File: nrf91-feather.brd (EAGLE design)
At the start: 50.8 x 22.9 mm, 125 parts, among them J1 CON-USB-1050170001, J2 CON-HEADER-1X12-MALE-PIN, J3 CON-HEADER-1X16-MALE-PIN, J4 CON-1909763-1, J5 CON-SIM-104224-0820, J6 CON-S2B-PH-SM4-TB(LF)(SN), J7 CON-1909763-1, J9 CON-TC2030-MCP-NL, Q1 MOSFET-P-SC89, Q2 MOSFET-DUAL-COMP-SOT563, Q3 MOSFET-P-20V-4.7A-SOT23, Q4 MOSFET-N-SC89, Q5 MOSFET-N-SC89, SW1 SW-EVP-AA402W, SW2 SW-EVP-AA402W, U1 MOD-NRF9160-SICA-R, U10 IC-LIS2DH12TR, U2 IC-CP2102N-A02-GQFN20R, U3 IC-TPS63031DSKR, U4 POWER-SWITCH-MIC94092YC6, U5 IC-TPD4S012DRYR, U6 FLASH-W25Q32JVZPIQ-WSON, U7 IC-STBC08PMR, U8 IC-PCF85063ATL/1, U9 IC-BAV70S, Y1 XTAL-ABS07AIG-32.768KHZ-7-T

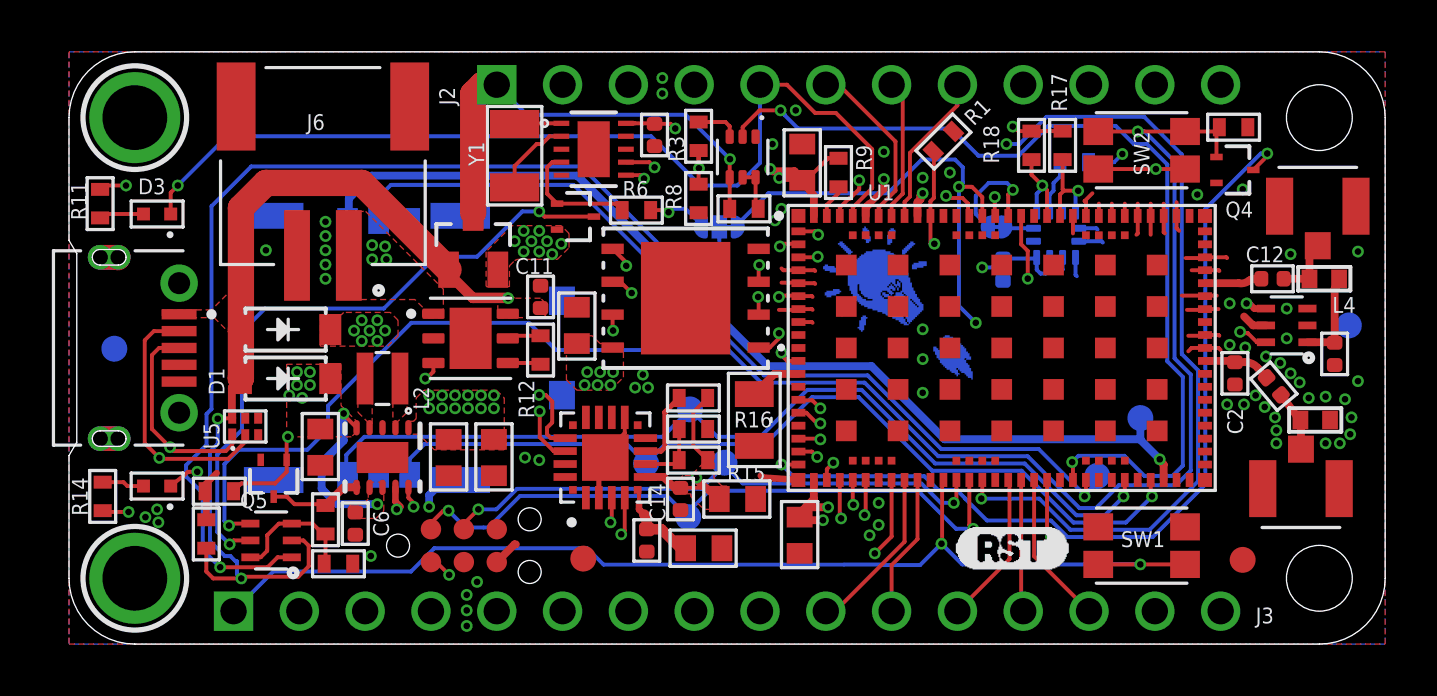
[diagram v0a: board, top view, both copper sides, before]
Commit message: Adding accelerometer INT2 pin connection.
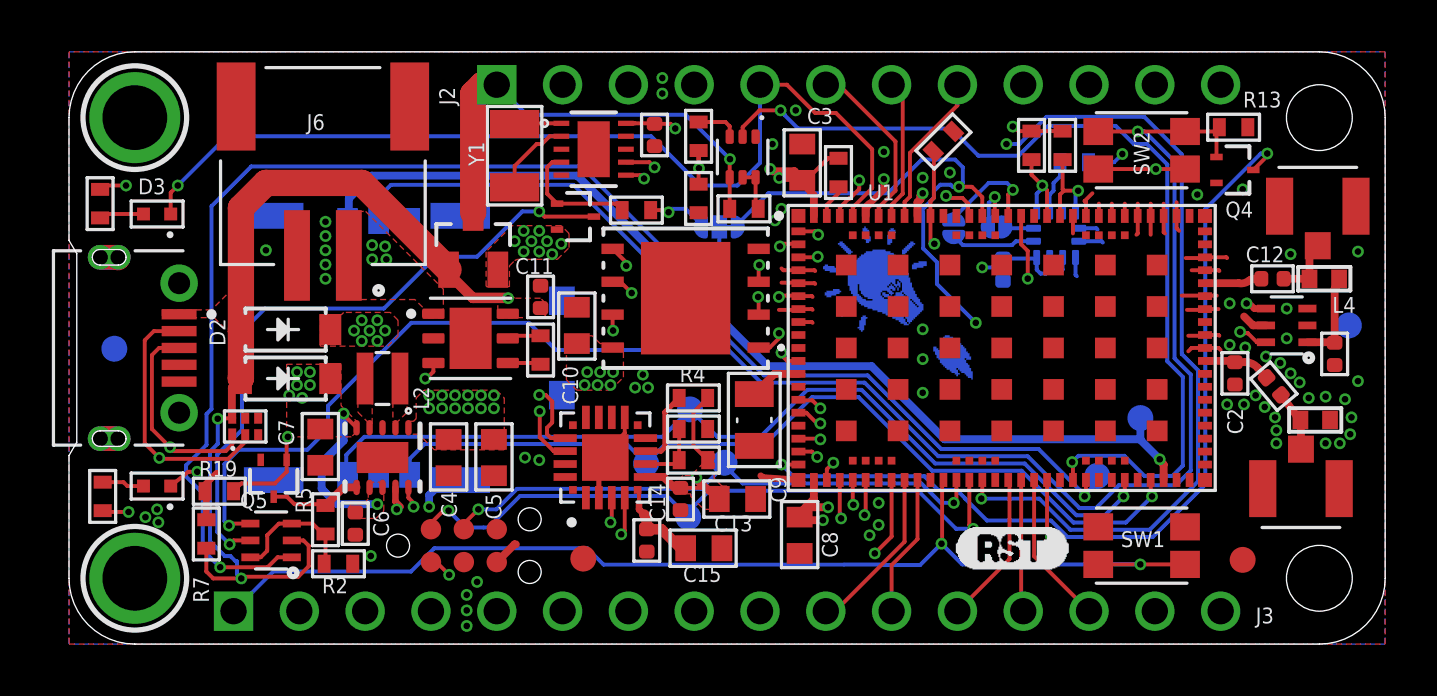
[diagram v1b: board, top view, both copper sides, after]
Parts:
- added JMP3: JUMPER-NO-ROUND-NO, wolff-den:JUMPER-ROUND-N0
- JMP1: value JUMPER-NC -> JUMPER-NO-ROUND-NO; device wolff-den:JUMPER-ROUND-NC -> wolff-den:JUMPER-ROUND-N0
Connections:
- new net N$12: JMP3.P$1, U10.11
- net P0.29/D2: now also JMP3.P$2; no longer JMP1.P$2
- net P0.30/D3: now also JMP1.P$2
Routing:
- net N$12: track 0.00 -> 3.28 mm
- net P0.31/NRF_PS_EN: track 33.7 -> 35.3 mm
- net P0.30/D3: track 5.98 -> 7.24 mm

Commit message: Optimizing power layout
Changed:
* Created large power paths on middle layers (power an return)
* Pin7 on power supply chip to ground (power save mode/pfm enabled)
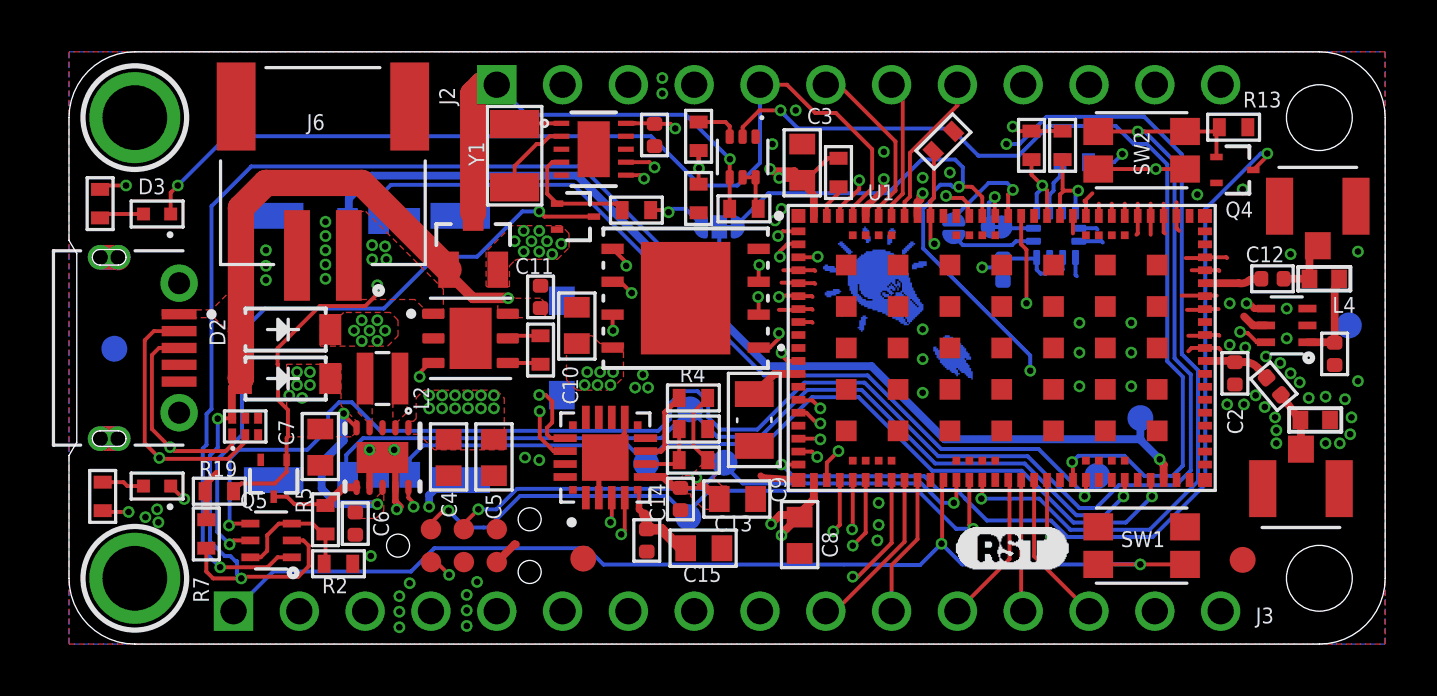
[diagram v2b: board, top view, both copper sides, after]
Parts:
- JMP1: value JUMPER-NO-ROUND-NO -> JUMPER-NC; device wolff-den:JUMPER-ROUND-N0 -> wolff-den:JUMPER-ROUND-NC
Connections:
- net GND: now also U3.7
- net VSYS: no longer U3.7
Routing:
- net GND: track 44.8 -> 47.1 mm, vias 68 -> 82
- net P0.13/A0: track 16.1 -> 18.3 mm
- net VBUS: track 55.1 -> 53.7 mm
- net P0.05/USB_UART_RX: track 19.4 -> 17.9 mm
- net DIFF_P: track 28.5 -> 27.1 mm
- net DIFF_N: track 31.8 -> 30.6 mm
- net !EN: track 22.6 -> 23.7 mm
- net FLASH_SO: track 13.9 -> 14.8 mm
- net MODE/WAKE: track 73.6 -> 74.2 mm
- net P0.16/A3: track 10.5 -> 9.91 mm
- net FLASH_WP: track 9.42 -> 8.85 mm
- net NRF_PS_EN_JMP: track 40.2 -> 39.6 mm

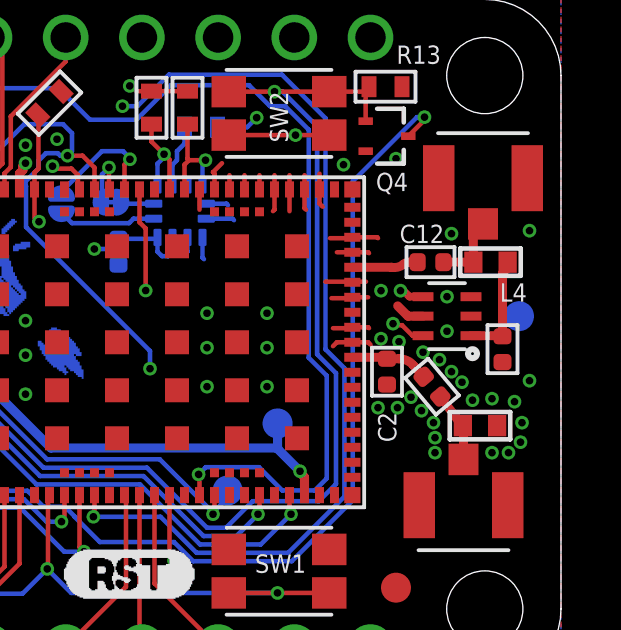
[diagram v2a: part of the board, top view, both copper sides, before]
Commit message: Replacing U4 with 2.8V regulator.
Changed:
* U4 to MIC5365-2.8YC5-TR
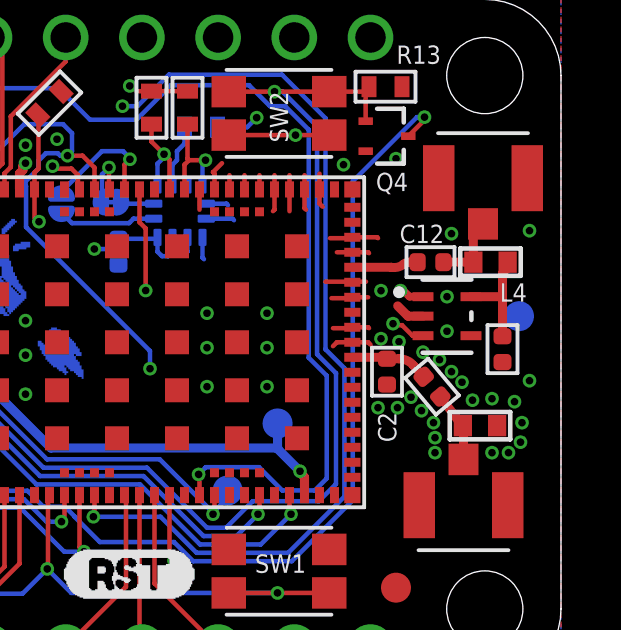
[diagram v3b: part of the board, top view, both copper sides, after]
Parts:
- U4: value POWER-SWITCH-MIC94092YC6 -> (none); device wolff-den:SOT363 -> wolff-den:SOT353
- turned U4 to 0 degrees
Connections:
- net +3V3: now also U4.1; no longer U4.4
- net COEX0/LNA_EN: now also U4.3; no longer U4.6
- net GND: no longer U4.5
- net LNA_SW_OUT: now also U4.5; no longer U4.1
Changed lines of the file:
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@@
 <layer number="29" name="tStop" color="7" fill="3" visible="no" active="yes"/>
 <layer number="30" name="bStop" color="7" fill="6" visible="no" active="yes"/>
-<layer number="31" name="tCream" color="7" fill="4" visible="no" active="yes"/>
+<layer number="31" name="tCream" color="7" fill="4" visible="yes" active="yes"/>
 <layer number="32" name="bCream" color="7" fill="5" visible="no" active="yes"/>
 <layer number="33" name="tFinish" color="6" fill="3" visible="no" active="yes"/>
@@
 <layer number="49" name="Reference" color="7" fill="1" visible="no" active="yes"/>
 <layer number="50" name="dxf" color="7" fill="1" visible="no" active="no"/>
-<layer number="51" name="tDocu" color="7" fill="1" visible="yes" active="yes"/>
+<layer number="51" name="tDocu" color="7" fill="1" visible="no" active="yes"/>
 <layer number="52" name="bDocu" color="7" fill="1" visible="no" active="yes"/>
 <layer number="53" name="tGND_GNDA" color="7" fill="9" visible="no" active="no"/>
@@
 <attribute name="TOLERANCE" value="5%" x="5.8" y="5.9" size="1.778" layer="27" display="off"/>
 </element>
-<element name="U4" library="wolff-den" library_urn="urn:adsk.eagle:library:6370453" package="SOT363" package3d_urn="urn:adsk.eagle:package:5807345/9" value="POWER-SWITCH-MIC94092YC6" x="47" y="12.3" smashed="yes" rot="R90">
-<attribute name="DESC" value="IC LOAD SW HGH SIDE 1.2A SC70-6" x="47" y="12.3" size="1.778" layer="27" rot="R90" display="off"/>
-<attribute name="DIGIKEYPN" value="576-3488-1-ND" x="47" y="12.3" size="1.778" layer="27" rot="R90" display="off"/>
-<attribute name="MPN" value="MIC94092YC6-TR" x="47" y="12.3" size="1.778" layer="27" rot="R90" display="off"/>
-<attribute name="NAME" x="45.0465" y="12.34428125" size="0.6096" layer="25" font="vector" ratio="20" rot="R90"/>
-<attribute name="NAME" x="47" y="12.3" size="0.2" layer="51" rot="R90" align="center"/>
+<element name="U4" library="wolff-den" library_urn="urn:adsk.eagle:library:6370453" package="SOT353" package3d_urn="urn:adsk.eagle:package:19061981/1" value="" x="47" y="12.3" smashed="yes">
+<attribute name="DESC" value="IC REG LINEAR 2.8V 150MA SC70-5" x="47" y="12.3" size="1.778" layer="27" display="off"/>
+<attribute name="DIGIKEYPN" value="576-3187-1-ND" x="47" y="12.3" size="1.778" layer="27" display="off"/>
+<attribute name="MPN" value="MIC5365-2.8YC5-TR" x="47" y="12.3" size="1.778" layer="27" display="off"/>
+<attribute name="NAME" x="45.0965" y="11.89428125" size="0.6096" layer="25" font="vector" ratio="20" rot="R90"/>
+<attribute name="NAME" x="47" y="12.3" size="0.2" layer="51" align="center"/>
 </element>
 <element name="C2" library="wolff-den" library_urn="urn:adsk.eagle:library:6370453" package="CAPC1005X55N" package3d_urn="urn:adsk.eagle:package:7419912/5" value="15p" x="45" y="10.45" smashed="yes" rot="R270">
@@
 <wire x1="5.25" y1="5.9" x2="5.25" y2="6.15" width="0.254" layer="1"/>
 <wire x1="5.25" y1="6.15" x2="5.7" y2="6.6" width="0.254" layer="1"/>
-<contactref element="U4" pad="5"/>
 <contactref element="U4" pad="2"/>
 <via x="44.8" y="13.15" extent="1-16" drill="0.254"/>
@@
 <wire x1="36.45" y1="20" x2="36.425" y2="19.975" width="0.1524" layer="1"/>
 <via x="36.425" y="19.975" extent="1-16" drill="0.254"/>
-<contactref element="U4" pad="4"/>
+<contactref element="U4" pad="1"/>
 <wire x1="45.45" y1="13.15" x2="45.55" y2="13.15" width="0.254" layer="1"/>
 <wire x1="45.75" y1="12.95" x2="45.55" y2="13.15" width="0.254" layer="1"/>
@@
 <wire x1="33.4" y1="15.45" x2="33.8794" y2="14.9706" width="0.1524" layer="2"/>
 <contactref element="R1" pad="2"/>
-<contactref element="U4" pad="6"/>
+<contactref element="U4" pad="3"/>
 <wire x1="46.2" y1="11.65" x2="45.85" y2="11.65" width="0.1524" layer="1"/>
 <wire x1="45.2" y1="12.05" x2="45.1842" y2="12.05" width="0.1524" layer="2"/>
@@
 <contactref element="L4" pad="1"/>
 <contactref element="C19" pad="1"/>
-<contactref element="U4" pad="1"/>
+<contactref element="U4" pad="5"/>
 <wire x1="49.11075" y1="14.01075" x2="49.11075" y2="13.98925" width="0.254" layer="1"/>
 <wire x1="48.85" y1="11.63" x2="48.83" y2="11.65" width="0.3" layer="1"/>
-<wire x1="48.83" y1="11.65" x2="47.8" y2="11.65" width="0.3" layer="1"/>
 <wire x1="49.11075" y1="13.98925" x2="48.85" y2="13.7285" width="0.3" layer="1"/>
-<wire x1="48.85" y1="11.63" x2="48.85" y2="13.7285" width="0.3" layer="1"/>
+<wire x1="48.85" y1="11.63" x2="48.85" y2="12.95" width="0.3" layer="1"/>
+<wire x1="48.85" y1="12.95" x2="48.85" y2="13.7285" width="0.3" layer="1"/>
 <wire x1="49.0215" y1="14.1" x2="49.11075" y2="14.01075" width="0.3" layer="1"/>
+<wire x1="47.8" y1="12.95" x2="48.85" y2="12.95" width="0.3" layer="1"/>
 </signal>
 <signal name="GPS_ANT" class="2">

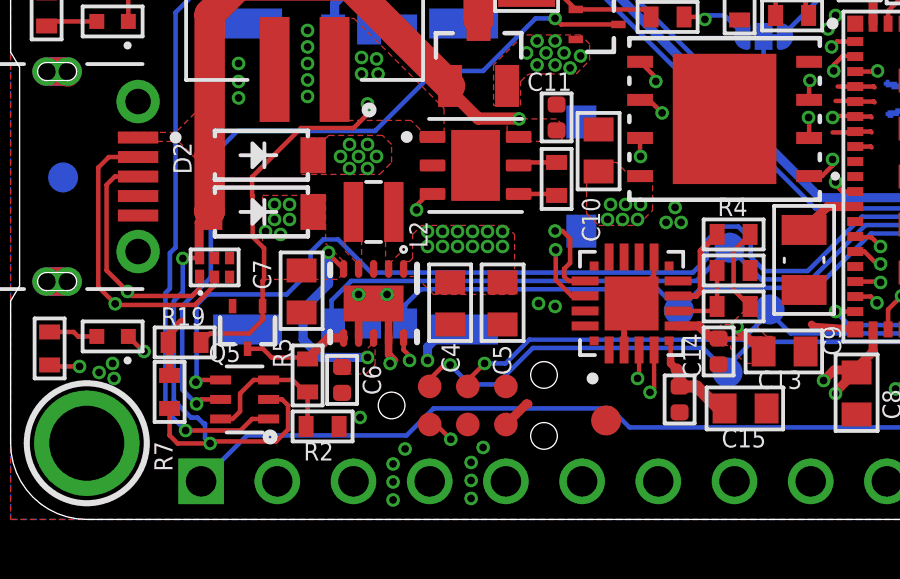
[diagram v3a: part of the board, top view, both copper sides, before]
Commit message: Comparing and fixing U3 connections
Changed:
* U3.8 should not be connected to VSYS. Now the same as a few reference designs i've seen.
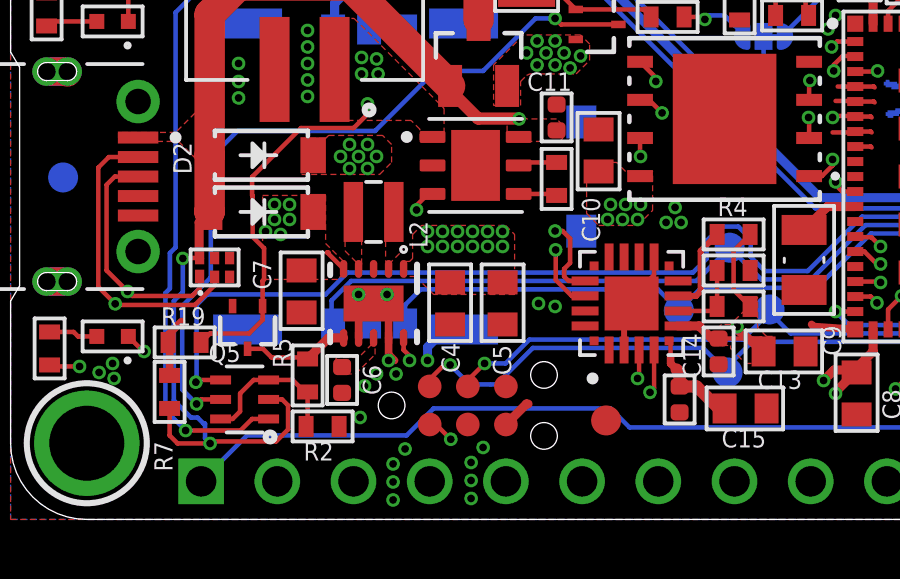
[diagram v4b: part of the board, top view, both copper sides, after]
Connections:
- new net N$14: C6.1, U3.8
- net VSYS: no longer C6.1, U3.8
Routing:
- net VSYS: track 60.7 -> 54.0 mm, vias 20 -> 18
- net MODE/WAKE: track 74.2 -> 72.9 mm
- net GND: vias 82 -> 85
- added copper zone on layer 1, net N$14
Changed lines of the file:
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@@
 <layer number="29" name="tStop" color="7" fill="3" visible="no" active="yes"/>
 <layer number="30" name="bStop" color="7" fill="6" visible="no" active="yes"/>
-<layer number="31" name="tCream" color="7" fill="4" visible="yes" active="yes"/>
+<layer number="31" name="tCream" color="7" fill="4" visible="no" active="yes"/>
 <layer number="32" name="bCream" color="7" fill="5" visible="no" active="yes"/>
 <layer number="33" name="tFinish" color="6" fill="3" visible="no" active="yes"/>
@@
 <layer number="49" name="Reference" color="7" fill="1" visible="no" active="yes"/>
 <layer number="50" name="dxf" color="7" fill="1" visible="no" active="no"/>
-<layer number="51" name="tDocu" color="7" fill="1" visible="no" active="yes"/>
+<layer number="51" name="tDocu" color="7" fill="1" visible="yes" active="yes"/>
 <layer number="52" name="bDocu" color="7" fill="1" visible="no" active="yes"/>
 <layer number="53" name="tGND_GNDA" color="7" fill="9" visible="no" active="no"/>
@@
 <via x="21.85" y="9.9" extent="1-16" drill="0.254"/>
 <via x="22.15" y="10.4" extent="1-16" drill="0.254"/>
-<via x="12.65" y="5.2" extent="1-16" drill="0.254"/>
+<via x="12.6" y="5.3" extent="1-16" drill="0.254"/>
 <via x="11.65" y="3.4" extent="1-16" drill="0.254"/>
 <wire x1="30.75" y1="16.525" x2="30.75" y2="16.8471" width="0.3048" layer="1"/>
@@
 <via x="7.6" y="14.6" extent="1-16" drill="0.254"/>
 <via x="7.6" y="14.05" extent="1-16" drill="0.254"/>
+<via x="12.2" y="4.85" extent="1-16" drill="0.254"/>
+<via x="11.8" y="4.45" extent="1-16" drill="0.254"/>
+<via x="12.85" y="4.85" extent="1-16" drill="0.254"/>
 </signal>
 <signal name="+3V3">
@@
 <contactref element="D1" pad="1"/>
 <contactref element="C7" pad="1"/>
-<contactref element="C6" pad="1"/>
 <contactref element="U3" pad="5"/>
-<contactref element="U3" pad="8"/>
-<via x="11.9" y="5.4" extent="1-16" drill="0.254"/>
 <polygon width="0.1524" layer="1" thermals="no">
 <vertex x="10.9" y="8"/>
@@
 <via x="19" y="15.45" extent="1-16" drill="0.254"/>
 <via x="8.5" y="9.6" extent="1-16" drill="0.254"/>
-<polygon width="0.1524" layer="1" thermals="no">
-<vertex x="10.85" y="5.4"/>
-<vertex x="10.85" y="4.85"/>
-<vertex x="11.85" y="4.85"/>
-<vertex x="12.15" y="5.15"/>
-<vertex x="12.15" y="6.25"/>
-<vertex x="12.05" y="6.25"/>
-<vertex x="12.05" y="5.85"/>
-<vertex x="11.6" y="5.4"/>
-</polygon>
 <contactref element="SW2" pad="3"/>
 <contactref element="SW2" pad="1"/>
@@
 <wire x1="11.100003125" y1="8.35" x2="10.550003125" y2="8.9" width="0.1524" layer="1"/>
 <wire x1="10.550003125" y1="8.9" x2="10.6" y2="8.9" width="0.1524" layer="1"/>
-<via x="10.6" y="8.9" extent="1-16" drill="0.254"/>
-<wire x1="10.6" y1="8.9" x2="10.6" y2="7.85" width="0.3048" layer="16"/>
-<wire x1="10.6" y1="7.85" x2="9.75" y2="7" width="0.3048" layer="16"/>
-<wire x1="9.75" y1="7" x2="9.75" y2="6" width="0.3048" layer="16"/>
-<wire x1="10.35" y1="5.4" x2="11.9" y2="5.4" width="0.3048" layer="16"/>
-<wire x1="9.75" y1="6" x2="10.35" y2="5.4" width="0.3048" layer="16"/>
-<wire x1="10.6" y1="8.9" x2="10.6" y2="9.95" width="0.3048" layer="2"/>
 <wire x1="10.6" y1="9.95" x2="10.65" y2="10" width="0.3048" layer="2"/>
 <wire x1="23.1742625" y1="16.7" x2="23.1424625" y2="16.6682" width="0.1524" layer="16"/>
@@
 <wire x1="42.6706" y1="18.6294" x2="41.515" y2="19.785" width="0.1524" layer="16"/>
 <wire x1="41.515" y1="19.785" x2="41.25" y2="19.785" width="0.1524" layer="16"/>
-<wire x1="10" y1="8.9106625" x2="10" y2="8.3" width="0.1524" layer="16"/>
 <wire x1="6.2" y1="7.15" x2="6.55" y2="7.5" width="0.1524" layer="16"/>
-<wire x1="6.55" y1="7.5" x2="9.2" y2="7.5" width="0.1524" layer="16"/>
-<wire x1="9.2" y1="7.5" x2="10" y2="8.3" width="0.1524" layer="16"/>
+<wire x1="6.55" y1="7.5" x2="10.5" y2="7.5" width="0.1524" layer="16"/>
+<wire x1="10.5" y1="7.5" x2="11.2294" y2="8.2294" width="0.1524" layer="16"/>
 <contactref element="J3" pad="3"/>
 <wire x1="24.670875" y1="9.3497" x2="24.25895" y2="9.761625" width="0.1524" layer="16"/>
@@
 <wire x1="23.6764" y1="9.761625" x2="23.2" y2="9.285225" width="0.1524" layer="16"/>
 <wire x1="23.2" y1="8.6858875" x2="22.7435125" y2="8.2294" width="0.1524" layer="16"/>
-<wire x1="22.7435125" y1="8.2294" x2="12.0206" y2="8.2294" width="0.1524" layer="16"/>
-<wire x1="10.4211375" y1="9.3318" x2="10" y2="8.9106625" width="0.1524" layer="16"/>
-<wire x1="10.9182" y1="9.3318" x2="10.4211375" y2="9.3318" width="0.1524" layer="16"/>
-<wire x1="12.0206" y1="8.2294" x2="10.9182" y2="9.3318" width="0.1524" layer="16"/>
+<wire x1="22.7435125" y1="8.2294" x2="11.2294" y2="8.2294" width="0.1524" layer="16"/>
 <wire x1="11.43" y1="1.27" x2="9.95" y2="2.75" width="0.1524" layer="2"/>
 <wire x1="8" y1="2.75" x2="6.175" y2="4.575" width="0.1524" layer="2"/>
@@
 <wire x1="36.4" y1="15.4" x2="34.5" y2="15.4" width="0.1524" layer="16"/>
 </signal>
+<signal name="N$14">
+<contactref element="C6" pad="1"/>
+<contactref element="U3" pad="8"/>
+<polygon width="0.1524" layer="1" thermals="no">
+<vertex x="10.85" y="5.4"/>
+<vertex x="10.85" y="4.85"/>
+<vertex x="11.5" y="4.85"/>
+<vertex x="12.15" y="5.5"/>
+<vertex x="12.15" y="6.25"/>
+<vertex x="12.05" y="6.25"/>
+<vertex x="12.05" y="5.85"/>
+<vertex x="11.6" y="5.4"/>
+</polygon>
+</signal>
 </signals>
